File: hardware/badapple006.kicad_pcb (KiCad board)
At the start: 2 copper layers, 16.4 x 16.2 mm, 35 parts, among them J1 OLED, J10 SCL, J11 SDA, J2 USB_C_Receptacle_USB2.0, J3 PG, J4 3.3, J5 GND, J6 RFO, J7 RFA, J8 APPLE, J9 RFO2, U1 CH32V006F8U6, U2 RS3236-3.3YUTDN4, Y1 24MHz

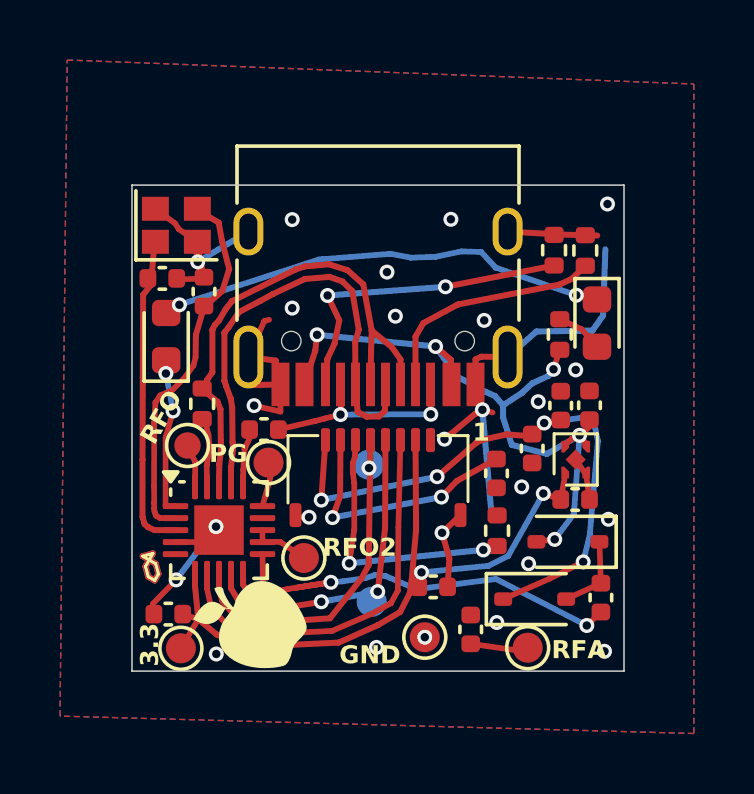
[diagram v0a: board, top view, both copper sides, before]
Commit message: Update with programming jig
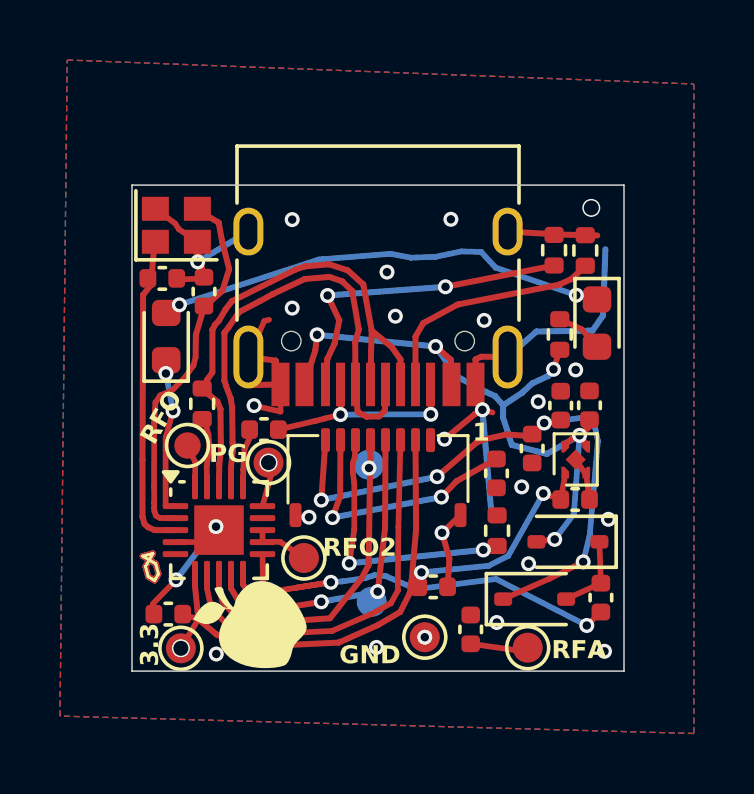
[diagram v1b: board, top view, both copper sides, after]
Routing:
- net SWIO: vias 0 -> 1
- net OVDD: vias 2 -> 3
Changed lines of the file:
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@@
+	)
+	(via
+		(at 71.63 95.44)
+		(size 0.6)
+		(drill 0.5)
+		(layers "F.Cu" "B.Cu")
+		(net 2)
 	)
 	(via
@@
 		(net 20)
 	)
+	(via
+		(at 74.55 89.25)
+		(size 0.6)
+		(drill 0.5)
+		(layers "F.Cu" "B.Cu")
+		(net 20)
+	)
 	(segment
 		(start 72.11 89.23)
@@
 	)
 	(via
-		(at 85.85 80.63)
-		(size 0.5)
-		(drill 0.28)
+		(at 85.31 80.76)
+		(size 0.6)
+		(drill 0.5)
 		(layers "F.Cu" "B.Cu")
 		(free yes)
@@
 			)
 		)
+	)
+	(zone
+		(net 0)
+		(net_name "")
+		(layer "F.Mask")
+		(hatch edge 0.5)
+		(connect_pads
+			(clearance 0.23)
+		)
+		(min_thickness 0.25)
+		(filled_areas_thickness no)
+		(fill yes
+			(thermal_gap 0.5)
+			(thermal_bridge_width 0.5)
+		)
+		(polygon
+			(pts
+				(xy 87.03 81.22) (xy 83.87 81.22) (xy 83.87 79.69) (xy 87.02 79.69)
+			)
+		)
